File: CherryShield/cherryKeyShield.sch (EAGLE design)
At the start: 19 parts

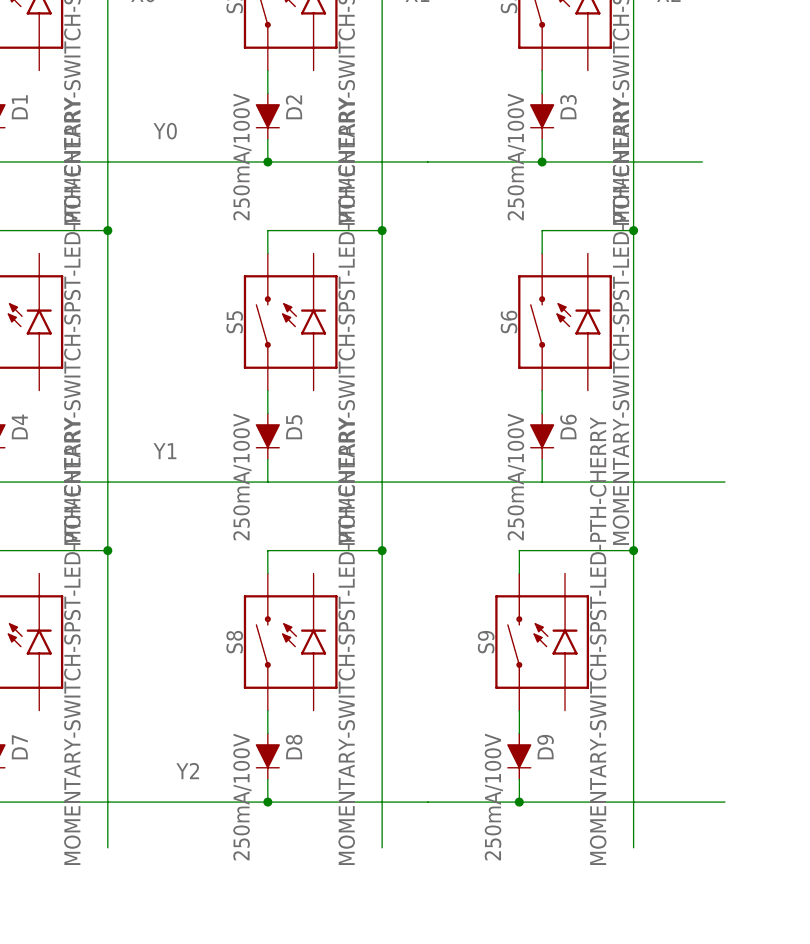
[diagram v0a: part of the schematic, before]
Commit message: minimized size for cost
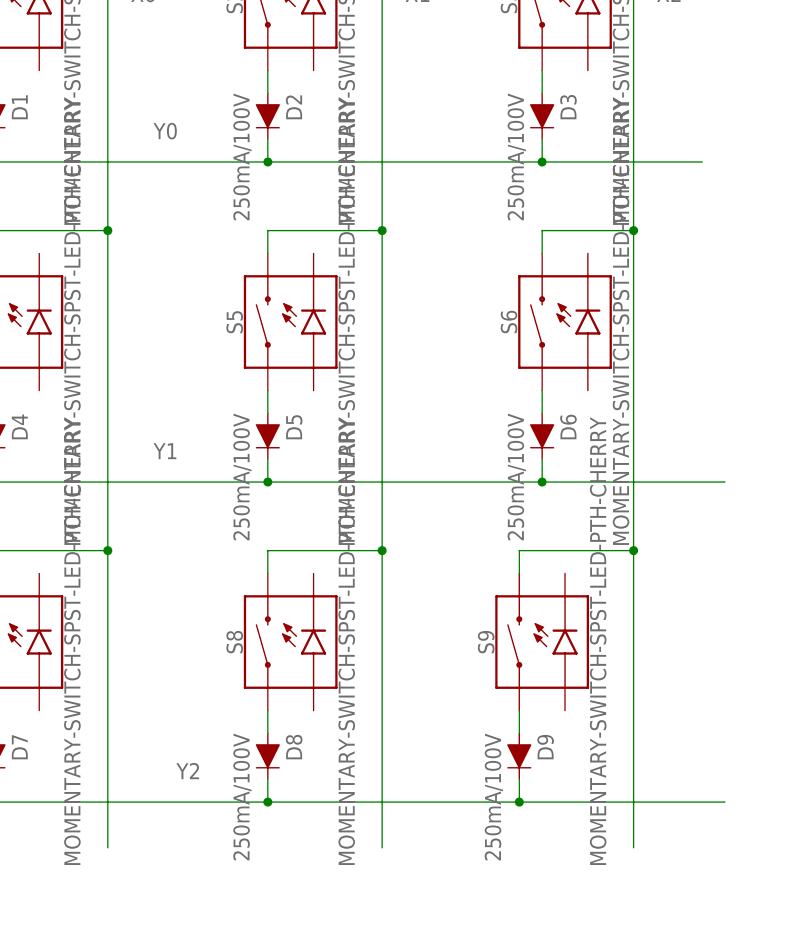
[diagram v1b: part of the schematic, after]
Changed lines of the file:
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@@
 <?xml version="1.0" encoding="utf-8"?>
 <!DOCTYPE eagle SYSTEM "eagle.dtd">
-<eagle version="8.2.1">
+<eagle version="8.2.2">
 <drawing>
 <settings>
@@
 <wire x1="27.94" y1="99.06" x2="58.42" y2="99.06" width="0.1524" layer="91"/>
 <pinref part="D1" gate="G$1" pin="C"/>
-<wire x1="58.42" y1="99.06" x2="76.2" y2="99.06" width="0.1524" layer="91"/>
+<wire x1="58.42" y1="99.06" x2="88.9" y2="99.06" width="0.1524" layer="91"/>
 <wire x1="27.94" y1="101.6" x2="27.94" y2="99.06" width="0.1524" layer="91"/>
 <pinref part="D2" gate="G$1" pin="C"/>
@@
 <junction x="58.42" y="99.06"/>
 <label x="45.72" y="101.6" size="1.778" layer="95"/>
-</segment>
-<segment>
-<wire x1="76.2" y1="99.06" x2="88.9" y2="99.06" width="0.1524" layer="91"/>
 <pinref part="D3" gate="G$1" pin="C"/>
 <wire x1="88.9" y1="99.06" x2="106.68" y2="99.06" width="0.1524" layer="91"/>
@@
 <wire x1="88.9" y1="66.04" x2="88.9" y2="63.5" width="0.1524" layer="91"/>
 <label x="45.72" y="66.04" size="1.778" layer="95"/>
+<junction x="58.42" y="63.5"/>
+<junction x="88.9" y="63.5"/>
 </segment>
 <segment>
@@
 <wire x1="27.94" y1="27.94" x2="58.42" y2="27.94" width="0.1524" layer="91"/>
 <pinref part="D7" gate="G$1" pin="C"/>
-<wire x1="58.42" y1="27.94" x2="76.2" y2="27.94" width="0.1524" layer="91"/>
+<wire x1="58.42" y1="27.94" x2="86.36" y2="27.94" width="0.1524" layer="91"/>
 <wire x1="27.94" y1="30.48" x2="27.94" y2="27.94" width="0.1524" layer="91"/>
 <pinref part="D8" gate="G$1" pin="C"/>
@@
 <junction x="58.42" y="27.94"/>
 <label x="48.26" y="30.48" size="1.778" layer="95"/>
-</segment>
-<segment>
-<wire x1="76.2" y1="27.94" x2="86.36" y2="27.94" width="0.1524" layer="91"/>
 <pinref part="D9" gate="G$1" pin="C"/>
 <wire x1="86.36" y1="27.94" x2="109.22" y2="27.94" width="0.1524" layer="91"/>
@@
 </sheet>
 </sheets>
+<errors>
+</errors>
 </schematic>
 </drawing>
